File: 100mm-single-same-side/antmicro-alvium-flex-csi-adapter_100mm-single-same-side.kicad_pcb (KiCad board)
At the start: 2 copper layers, 25.5 x 100.1 mm, 2 parts, among them J1 WE_687622100002_FLEX, J2 WE_687650100002_FLEX

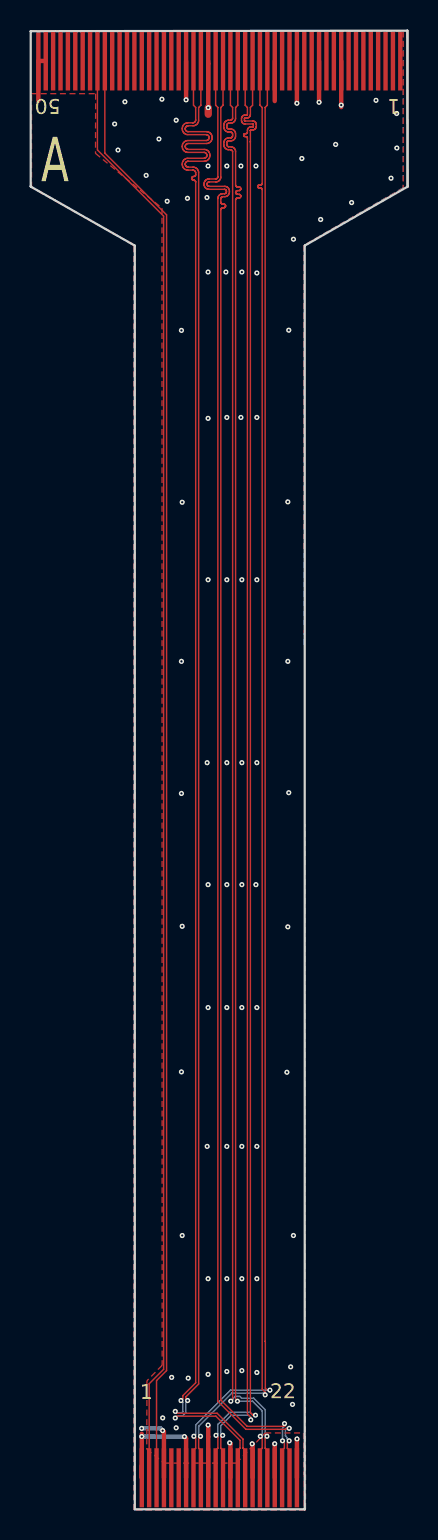
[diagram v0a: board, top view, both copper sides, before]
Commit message: Add NMOS transistor for camera triggering in 100mm single same side variant
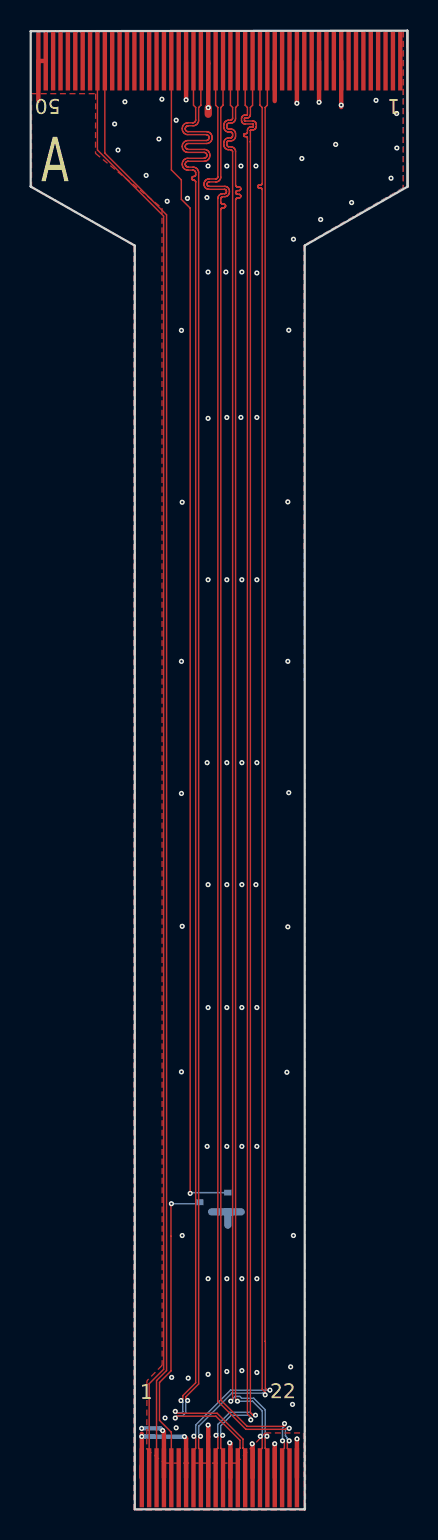
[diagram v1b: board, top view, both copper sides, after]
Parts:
- added Q1: BSS138APW, antmicro-alvium-flex-csi-adapter-footprints:SC70-3, B.Cu at (162.8, 144.0)
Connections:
- J2 pad 32: Net-(J2-Pad32) -> /VSYNC
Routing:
- net /VSYNC: track 0.00 -> 79.7 mm, vias 0 -> 1
- net /GPIO2: track 0.00 -> 21.2 mm, vias 0 -> 1
- net /GND: track 30.9 -> 33.8 mm

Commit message: 100mm-single-same: update signage
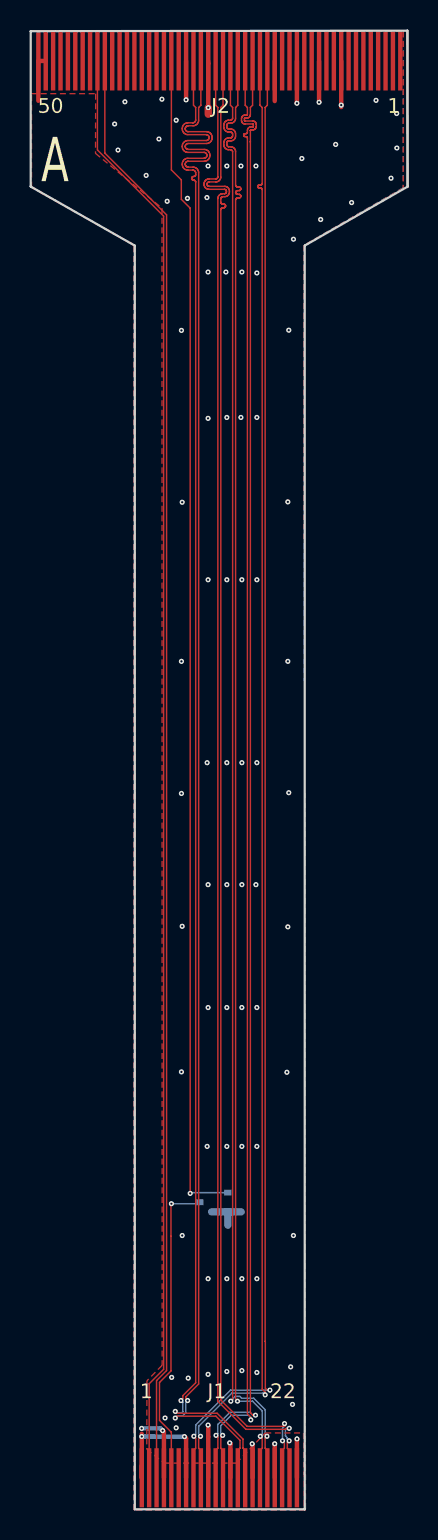
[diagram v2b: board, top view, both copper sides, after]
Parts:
- added N1: oshw_logo, antmicro-alvium-flex-csi-adapter-footprints:oshw-logo, B.Cu at (163.5, 132.5)
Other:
- board text added: "Antmicro Alvium Flex CSI Adapter 100mm single same side contacts Rev. 1.0.1"
- board text added: "LED ->"

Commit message: Remove obsolete markings
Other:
- board text removed: "A"
